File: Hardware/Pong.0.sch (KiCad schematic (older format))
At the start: 0 parts

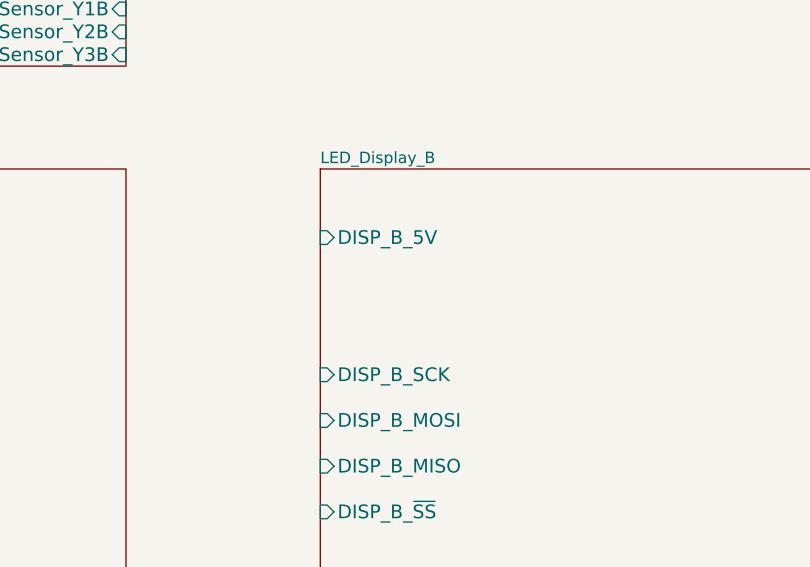
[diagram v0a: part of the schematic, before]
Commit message: Cleaned up RF Schematic Page
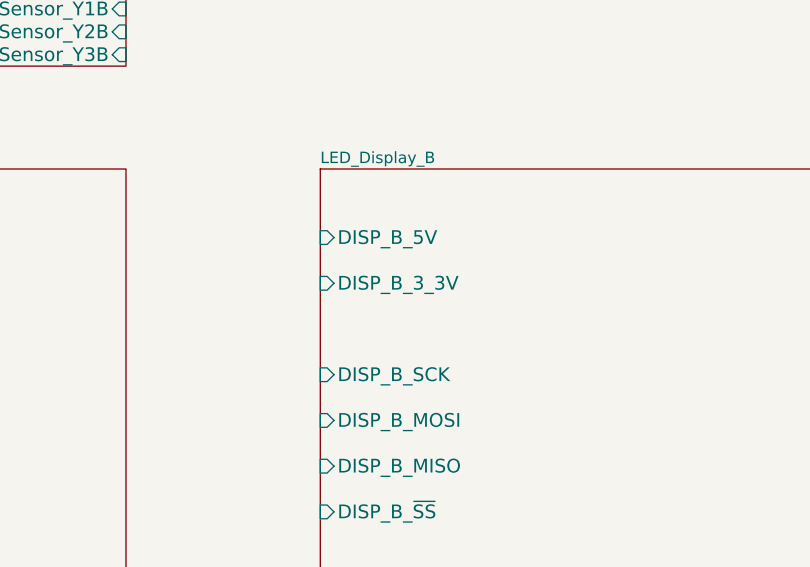
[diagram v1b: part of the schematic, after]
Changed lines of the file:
@@
 6E 56 52 49 51 4E 59 71 7E 65 C5 4D 0F AF 00 BF F6 21 9D BA 45 88 9C 00 16 00 C0 66 90 E0 00 00
 AC 42 3B 38 00 00 AB 90 E0 00 00 AC 42 82 03 00 B0 EA FF 00 E3 76 B5 A7 81 B6 BC 08 00 00 00 00
-49 45 4E 44 AE 42 60 82 FC $EndBitmap
+49 45 4E 44 AE 42 60 82 30 $EndBitmap
 EndData
 $EndBitmap
@@
 F5 "DISP_B_~SS" I L 11750 5050 60
 F6 "DISP_B_5V" I L 11750 3850 60
-$EndSheet
-$Sheet
+F7 "DISP_B_3_3V" I L 11750 4050 60
+$EndSheet
+$Sheet

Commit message: Non-critical changes
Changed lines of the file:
@@
 Sheet 1 7
 Title "Pong.0"
-Date "20 sep 2013"
+Date "24 sep 2013"
 Rev "0.3"
 Comp "Projects and Stuff LLC"
@@
 6E 56 52 49 51 4E 59 71 7E 65 C5 4D 0F AF 00 BF F6 21 9D BA 45 88 9C 00 16 00 C0 66 90 E0 00 00
 AC 42 3B 38 00 00 AB 90 E0 00 00 AC 42 82 03 00 B0 EA FF 00 E3 76 B5 A7 81 B6 BC 08 00 00 00 00
-49 45 4E 44 AE 42 60 82 30 $EndBitmap
+49 45 4E 44 AE 42 60 82 81 $EndBitmap
 EndData
 $EndBitmap
@@
 $EndSheet
 $Sheet
-S 11750 3550 2450 1800
+S 12050 3550 2450 1800
 U 523B2459
 F0 "LED_Display_B" 50
 F1 "LED_Display_B.sch" 50
-F2 "DISP_B_SCK" I L 11750 4450 60
-F3 "DISP_B_MOSI" I L 11750 4650 60
-F4 "DISP_B_MISO" I L 11750 4850 60
-F5 "DISP_B_~SS" I L 11750 5050 60
-F6 "DISP_B_5V" I L 11750 3850 60
-F7 "DISP_B_3_3V" I L 11750 4050 60
+F2 "DISP_B_SCK" I L 12050 4450 60
+F3 "DISP_B_MOSI" I L 12050 4650 60
+F4 "DISP_B_MISO" I L 12050 4850 60
+F5 "DISP_B_~SS" I L 12050 5050 60
+F6 "DISP_B_5V" I L 12050 3850 60
+F7 "DISP_B_3_3V" I L 12050 4050 60
 $EndSheet
 $Sheet
@@
 Text GLabel 2550 2750 0    60   Input ~ 0
 VBUS
+Text GLabel 11950 3850 0    60   Input ~ 0
+5V
+Text GLabel 11950 4050 0    60   Input ~ 0
+3_3V
+Text GLabel 8350 3900 0    60   Input ~ 0
+3_3V
+Text GLabel 8350 6100 0    60   Input ~ 0
+3_3V
+Text GLabel 2550 4600 0    60   Input ~ 0
+3_3V
+Wire Wire Line
+	2550 4600 2650 4600
+Wire Wire Line
+	11950 4050 12050 4050
+Wire Wire Line
+	11950 3850 12050 3850
+Wire Wire Line
+	8350 3900 8450 3900
+Wire Wire Line
+	8350 6100 8450 6100
 $EndSCHEMATC

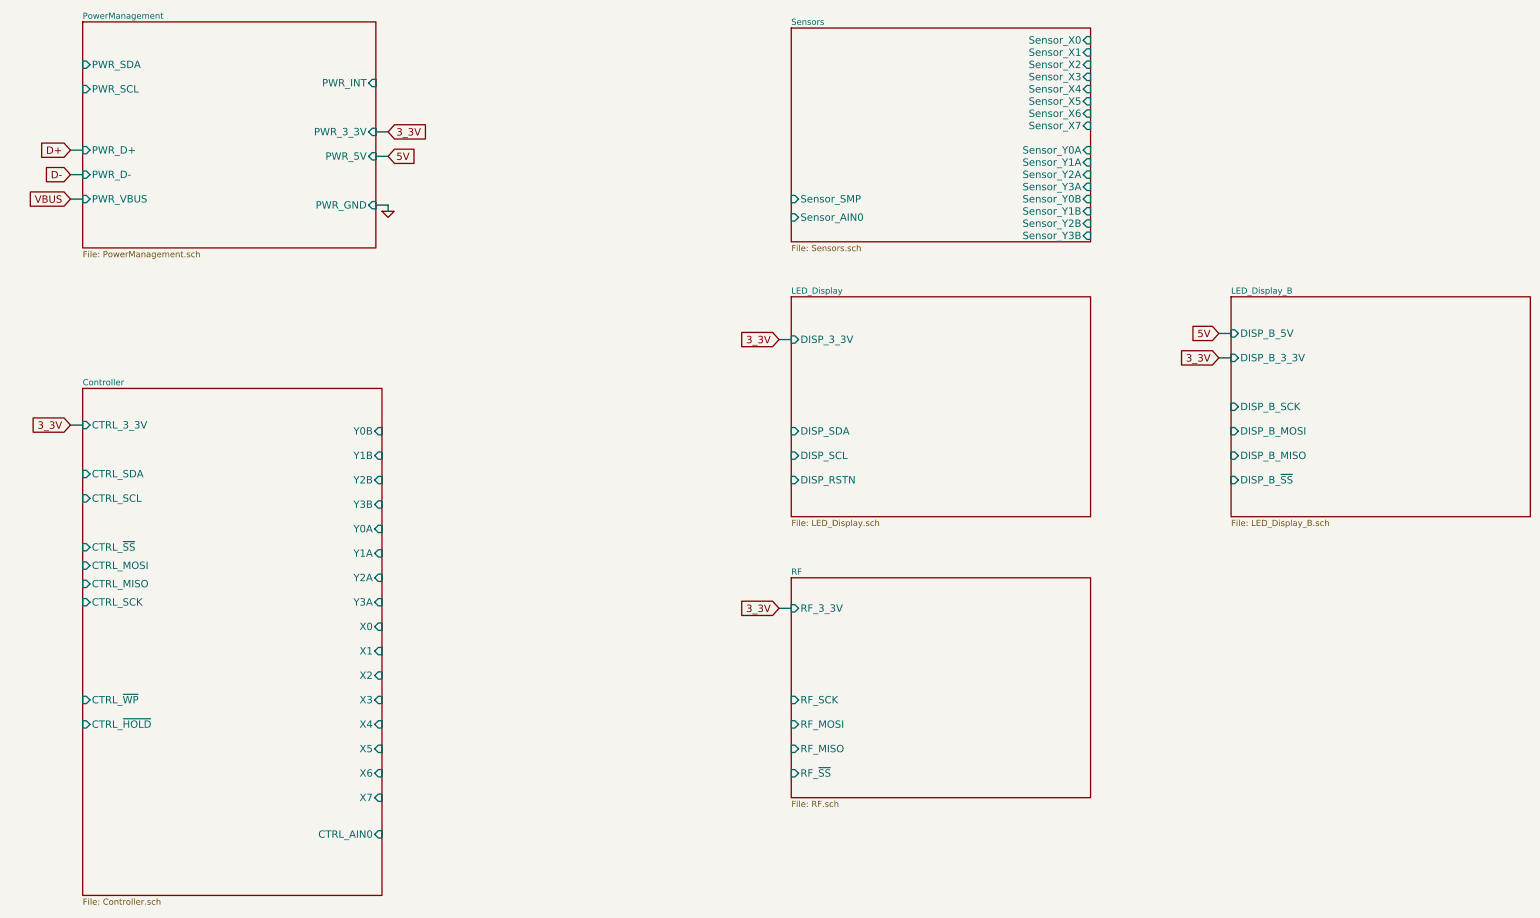
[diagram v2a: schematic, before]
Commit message: Began connecting major functional blocks
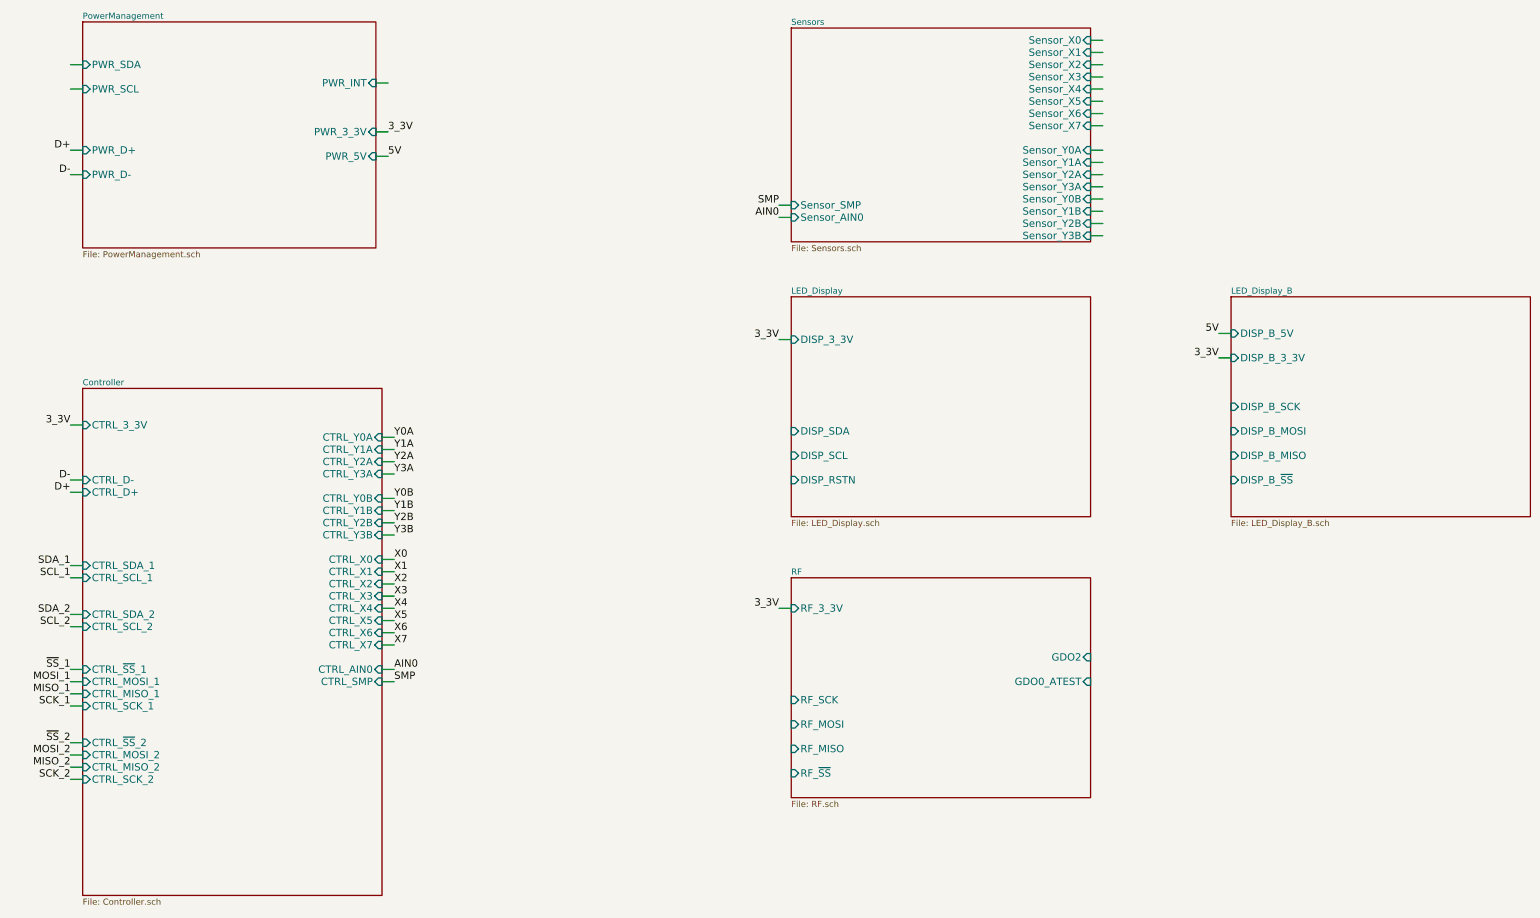
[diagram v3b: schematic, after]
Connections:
- net labels added: AIN0, MISO_1, MISO_2, MOSI_1, MOSI_2, SCK_1, SCK_2, SCL_1, SCL_2, SDA_1, SDA_2, SMP, X0, X1, X2, X3, X4, X5, X6, X7, Y0A, Y0B, Y1A, Y1B, Y2A, Y2B, Y3A, Y3B, ~SS~_1, ~SS~_2
- net labels removed: GND, VBUS
- wire segments 12 -> 62

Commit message: Minor misc changes
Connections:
- net labels added: GDO0, GDO2
- wire segments 62 -> 79
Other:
- note added: "CC2500\nRF Pins"
- note added: "QMatrix\nPins"
- note added: "USB\nPins"

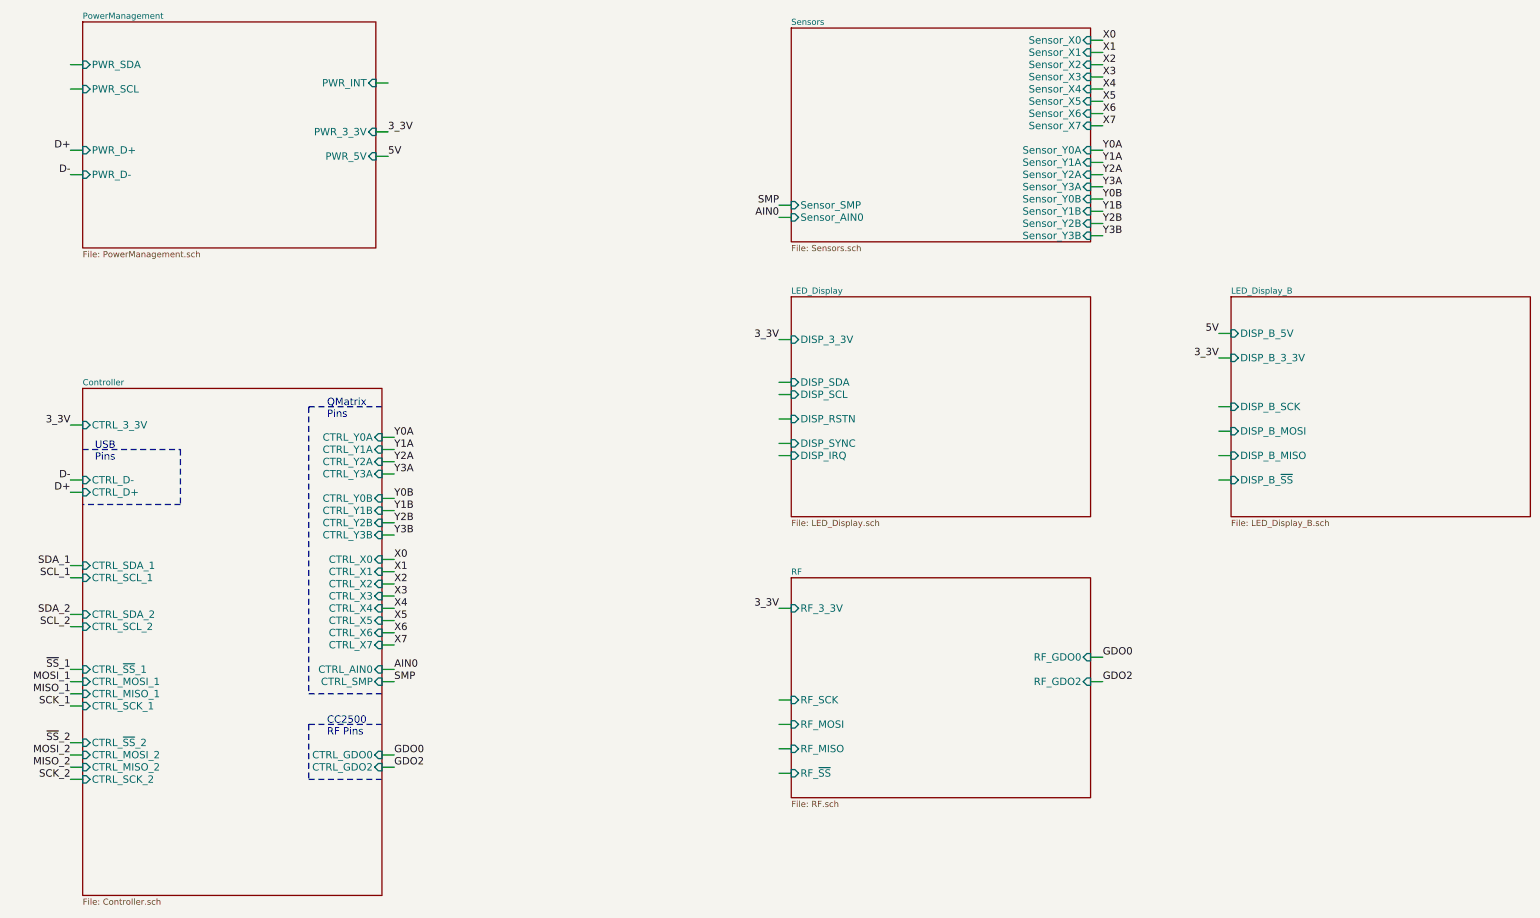
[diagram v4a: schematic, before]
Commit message: Cleaned up layout, and finalized pins
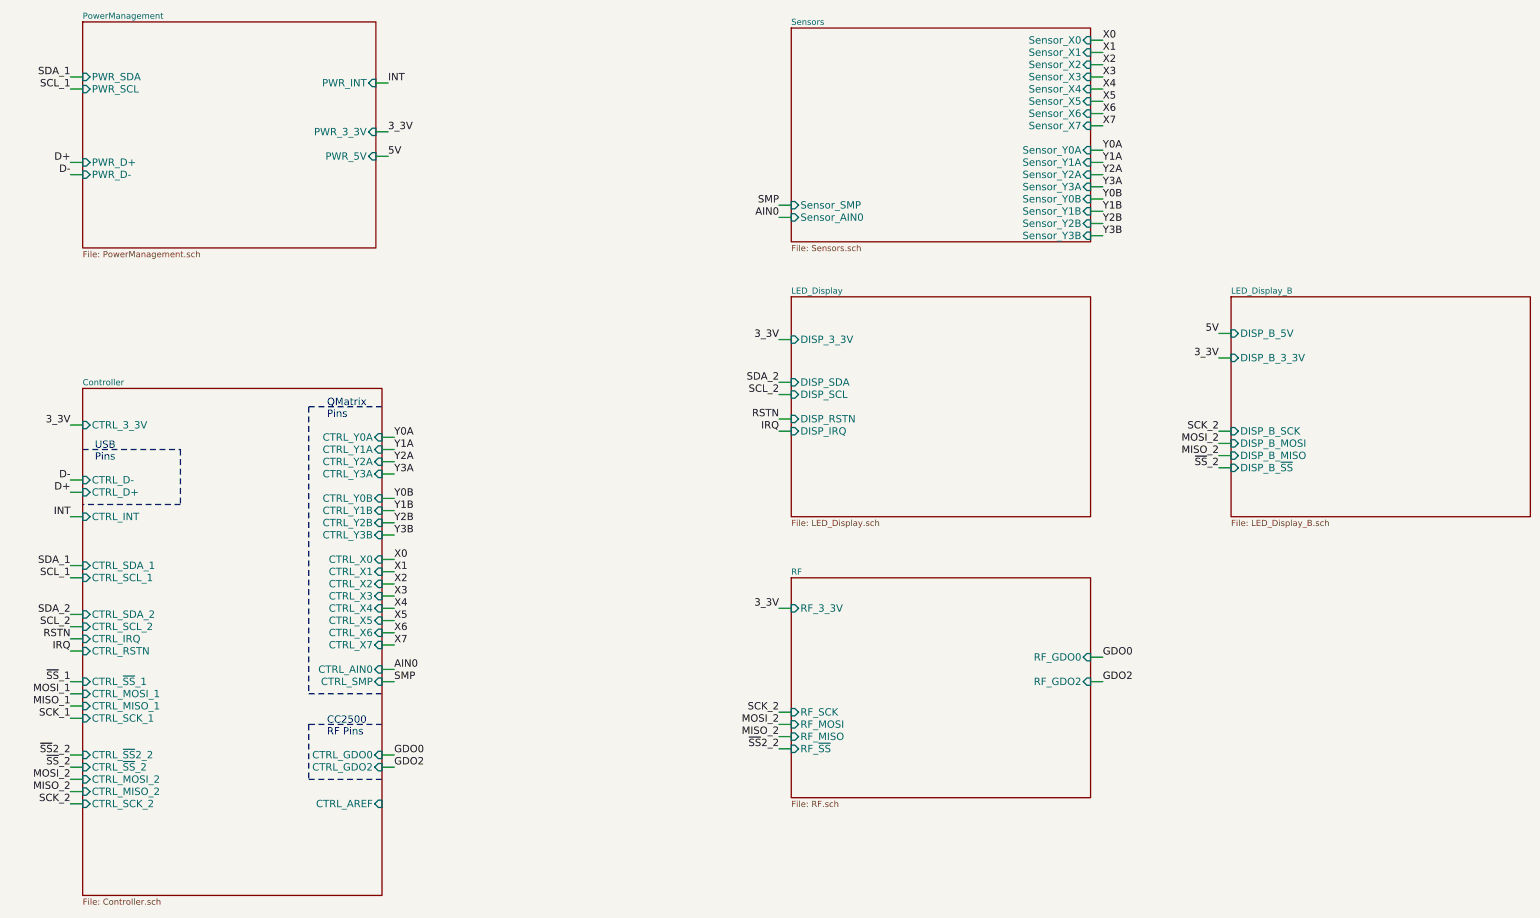
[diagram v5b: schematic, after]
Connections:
- net labels added: INT, IRQ, RSTN, ~SS~2_2
- wire segments 79 -> 82
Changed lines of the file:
@@
 Sheet 1 7
 Title "Pong.0"
-Date "25 sep 2013"
+Date "26 sep 2013"
 Rev "0.3"
 Comp "Projects and Stuff LLC"
@@
 6E 56 52 49 51 4E 59 71 7E 65 C5 4D 0F AF 00 BF F6 21 9D BA 45 88 9C 00 16 00 C0 66 90 E0 00 00
 AC 42 3B 38 00 00 AB 90 E0 00 00 AC 42 82 03 00 B0 EA FF 00 E3 76 B5 A7 81 B6 BC 08 00 00 00 00
-49 45 4E 44 AE 42 60 82 D7 $EndBitmap
+49 45 4E 44 AE 42 60 82 79 $EndBitmap
 EndData
 $EndBitmap
@@
 F0 "PowerManagement" 50
 F1 "PowerManagement.sch" 50
-F2 "PWR_SDA" I L 2650 1650 60
+F2 "PWR_SDA" I L 2650 1750 60
 F3 "PWR_SCL" I L 2650 1850 60
 F4 "PWR_D-" I L 2650 2550 60
-F5 "PWR_D+" I L 2650 2350 60
+F5 "PWR_D+" I L 2650 2450 60
 F6 "PWR_INT" I R 5050 1800 60
 F7 "PWR_3_3V" I R 5050 2200 60
@@
 F4 "DISP_RSTN" I L 8450 4550 60
 F5 "DISP_3_3V" I L 8450 3900 60
-F6 "DISP_SYNC" I L 8450 4750 60
-F7 "DISP_IRQ" I L 8450 4850 60
+F7 "DISP_IRQ" I L 8450 4650 60
 $EndSheet
 $Sheet
@@
 F0 "LED_Display_B" 50
 F1 "LED_Display_B.sch" 50
-F2 "DISP_B_SCK" I L 12050 4450 60
-F3 "DISP_B_MOSI" I L 12050 4650 60
+F2 "DISP_B_SCK" I L 12050 4650 60
+F3 "DISP_B_MOSI" I L 12050 4750 60
 F4 "DISP_B_MISO" I L 12050 4850 60
-F5 "DISP_B_~SS" I L 12050 5050 60
+F5 "DISP_B_~SS" I L 12050 4950 60
 F6 "DISP_B_5V" I L 12050 3850 60
 F7 "DISP_B_3_3V" I L 12050 4050 60
@@
 F1 "RF.sch" 50
 F2 "RF_3_3V" I L 8450 6100 60
-F3 "RF_SCK" I L 8450 6850 60
+F3 "RF_SCK" I L 8450 6950 60
 F4 "RF_MOSI" I L 8450 7050 60
-F5 "RF_MISO" I L 8450 7250 60
-F6 "RF_~SS" I L 8450 7450 60
+F5 "RF_MISO" I L 8450 7150 60
+F6 "RF_~SS" I L 8450 7250 60
 F7 "RF_GDO2" I R 10900 6700 60
 F8 "RF_GDO0" I R 10900 6500 60
@@
 	5050 2400 5150 2400
 Wire Wire Line
-	2550 2350 2650 2350
+	2550 2450 2650 2450
 Wire Wire Line
 	2550 2550 2650 2550
@@
 	2550 6250 2650 6250
 Wire Wire Line
-	2550 6600 2650 6600
-Wire Wire Line
 	2550 6700 2650 6700
 Wire Wire Line
@@
 	2550 6900 2650 6900
 Wire Wire Line
-	2550 7200 2650 7200
-Wire Wire Line
-	2550 7300 2650 7300
+	2550 7000 2650 7000
 Wire Wire Line
 	2550 7400 2650 7400
 Wire Wire Line
 	2550 7500 2650 7500
+Wire Wire Line
+	2550 7600 2650 7600
+Wire Wire Line
+	2550 7700 2650 7700
 Text Label 2550 5750 2    60   ~ 0
 SDA_1
@@
 Text Label 2550 6250 2    60   ~ 0
 SCL_2
-Text Label 2550 6600 2    60   ~ 0
+Text Label 2550 6700 2    60   ~ 0
 ~SS~_1
-Text Label 2550 6700 2    60   ~ 0
+Text Label 2550 6800 2    60   ~ 0
 MOSI_1
-Text Label 2550 6800 2    60   ~ 0
+Text Label 2550 6900 2    60   ~ 0
 MISO_1
-Text Label 2550 6900 2    60   ~ 0
+Text Label 2550 7000 2    60   ~ 0
 SCK_1
-Text Label 2550 7200 2    60   ~ 0
+Text Label 2550 7400 2    60   ~ 0
 ~SS~_2
-Text Label 2550 7300 2    60   ~ 0
+Text Label 2550 7500 2    60   ~ 0
 MOSI_2
-Text Label 2550 7400 2    60   ~ 0
+Text Label 2550 7600 2    60   ~ 0
 MISO_2
-Text Label 2550 7500 2    60   ~ 0
+Text Label 2550 7700 2    60   ~ 0
 SCK_2
 Text Label 2550 5050 2    60   ~ 0
@@
 Text Label 2550 5150 2    60   ~ 0
 D+
-Text Label 2550 2350 2    60   ~ 0
+Text Label 2550 2450 2    60   ~ 0
 D+
 Text Label 2550 2550 2    60   ~ 0
 D-
 Wire Wire Line
-	2550 1650 2650 1650
+	2550 1750 2650 1750
 Wire Wire Line
 	2550 1850 2650 1850
@@
 	8350 4550 8450 4550
 Wire Wire Line
-	11950 4450 12050 4450
-Wire Wire Line
-	11950 4650 12050 4650
-Wire Wire Line
-	11950 4850 12050 4850
-Wire Wire Line
-	11950 5050 12050 5050
-Wire Wire Line
 	11000 6500 10900 6500
 Wire Wire Line
 	11000 6700 10900 6700
 Wire Wire Line
-	8350 6850 8450 6850
+	8350 6950 8450 6950
 Wire Wire Line
 	8350 7050 8450 7050
 Wire Wire Line
+	8350 7150 8450 7150
+Wire Wire Line
 	8350 7250 8450 7250
 Wire Wire Line
-	8350 7450 8450 7450
-Wire Wire Line
-	8450 4750 8350 4750
-Wire Wire Line
-	8450 4850 8350 4850
+	8450 4650 8350 4650
 Text Label 11000 6500 0    60   ~ 0
 GDO0
@@
 F4 "CTRL_SDA_2" I L 2650 6150 60
 F5 "CTRL_SCL_2" I L 2650 6250 60
-F6 "CTRL_~SS~_2" I L 2650 7200 60
-F7 "CTRL_MOSI_2" I L 2650 7300 60
-F8 "CTRL_MISO_2" I L 2650 7400 60
-F9 "CTRL_SCK_2" I L 2650 7500 60
+F6 "CTRL_~SS~_2" I L 2650 7400 60
+F7 "CTRL_MOSI_2" I L 2650 7500 60
+F8 "CTRL_MISO_2" I L 2650 7600 60
+F9 "CTRL_SCK_2" I L 2650 7700 60
 F10 "CTRL_SDA_1" I L 2650 5750 60
 F11 "CTRL_SCL_1" I L 2650 5850 60
-F12 "CTRL_~SS~_1" I L 2650 6600 60
-F13 "CTRL_MOSI_1" I L 2650 6700 60
-F14 "CTRL_MISO_1" I L 2650 6800 60
-F15 "CTRL_SCK_1" I L 2650 6900 60
+F12 "CTRL_~SS~_1" I L 2650 6700 60
+F13 "CTRL_MOSI_1" I L 2650 6800 60
+F14 "CTRL_MISO_1" I L 2650 6900 60
+F15 "CTRL_SCK_1" I L 2650 7000 60
 F16 "CTRL_Y0B" I R 5100 5200 60
 F17 "CTRL_Y1B" I R 5100 5300 60
@@
 F35 "CTRL_GDO0" I R 5100 7300 60
 F36 "CTRL_GDO2" I R 5100 7400 60
+F37 "CTRL_AREF" I R 5100 7700 60
+F38 "CTRL_~SS~2_2" I L 2650 7300 60
+F39 "CTRL_INT" I L 2650 5350 60
+F40 "CTRL_IRQ" I L 2650 6350 60
+F41 "CTRL_RSTN" I L 2650 6450 60
 $EndSheet
 Text Notes 2750 4900 0    60   ~ 0
@@
 Text Label 5200 7400 0    60   ~ 0
 GDO2
+Wire Wire Line
+	2550 7300 2650 7300
+Text Label 2550 7300 2    60   ~ 0
+~SS~2_2
+Wire Wire Line
+	2650 5350 2550 5350
+Text Label 2550 5350 2    60   ~ 0
+INT
+Text Label 5150 1800 0    60   ~ 0
+INT
+Text Label 2550 1750 2    60   ~ 0
+SDA_1
+Text Label 2550 1850 2    60   ~ 0
+SCL_1
+Text Label 8350 4250 2    60   ~ 0
+SDA_2
+Text Label 8350 4350 2    60   ~ 0
+SCL_2
+Text Label 8350 4550 2    60   ~ 0
+RSTN
+Text Label 8350 4650 2    60   ~ 0
+IRQ
+Wire Wire Line
+	2550 6350 2650 6350
+Wire Wire Line
+	2650 6450 2550 6450
+Text Label 2550 6350 2    60   ~ 0
+RSTN
+Text Label 2550 6450 2    60   ~ 0
+IRQ
+Text Label 11950 4950 2    60   ~ 0
+~SS~_2
+Text Label 11950 4750 2    60   ~ 0
+MOSI_2
+Text Label 11950 4850 2    60   ~ 0
+MISO_2
+Text Label 11950 4650 2    60   ~ 0
+SCK_2
+Wire Wire Line
+	11950 4650 12050 4650
+Wire Wire Line
+	11950 4750 12050 4750
+Wire Wire Line
+	11950 4850 12050 4850
+Wire Wire Line
+	11950 4950 12050 4950
+Text Label 8350 7050 2    60   ~ 0
+MOSI_2
+Text Label 8350 7150 2    60   ~ 0
+MISO_2
+Text Label 8350 6950 2    60   ~ 0
+SCK_2
+Text Label 8350 7250 2    60   ~ 0
+~SS~2_2
 $EndSCHEMATC
